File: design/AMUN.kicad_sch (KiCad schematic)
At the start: 18 parts, among them IC2 SHT40-AD1B-R2, IC3 SGP40-D-R4, J6 SFV12R-1STBE1HLF, Q2 SSM3K16FV,L3F, U1 12P_ZIF_Connector, U2 ER-TFT018-3

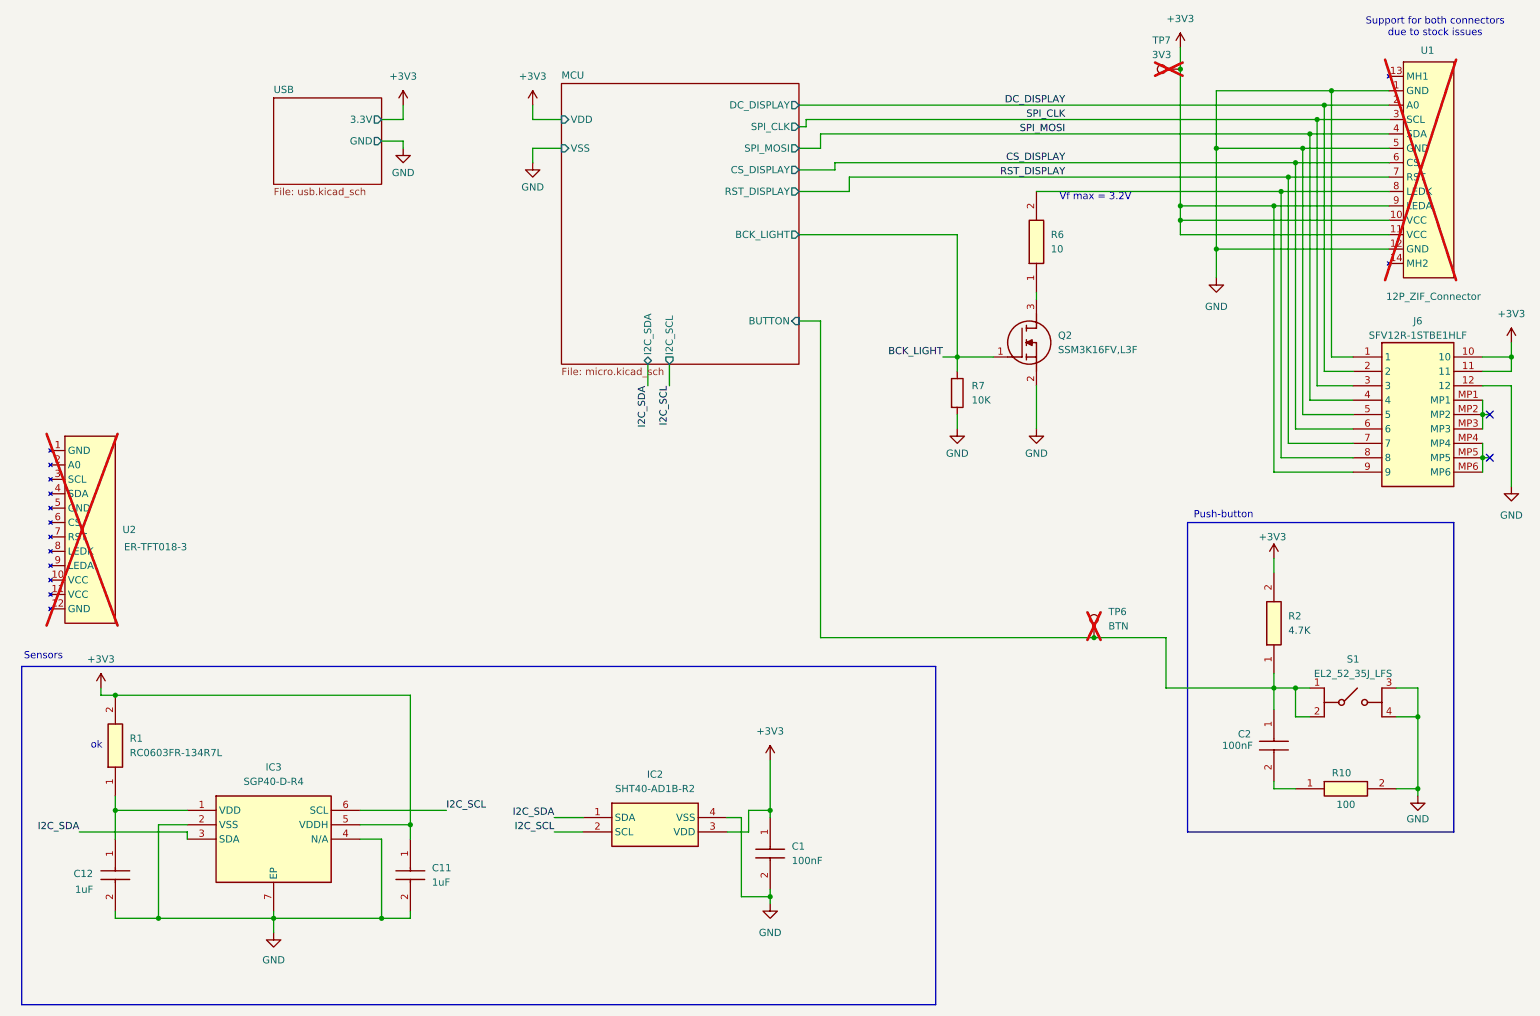
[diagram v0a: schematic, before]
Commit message: - Added display.kicad_sch; - Added mounting holes on schematic; - Removed TAG connect pads and used pin header; - Cut the PCB in order to make space for USB connector; - Changed mounting holes foorprint to non-plated ones; - Cut board near SHT4x sensor in order to reduce heat contribution from the rest of the board; - Re-routing; - Added revision number on silkscreen; - Shrunk components ID on silkscreen.
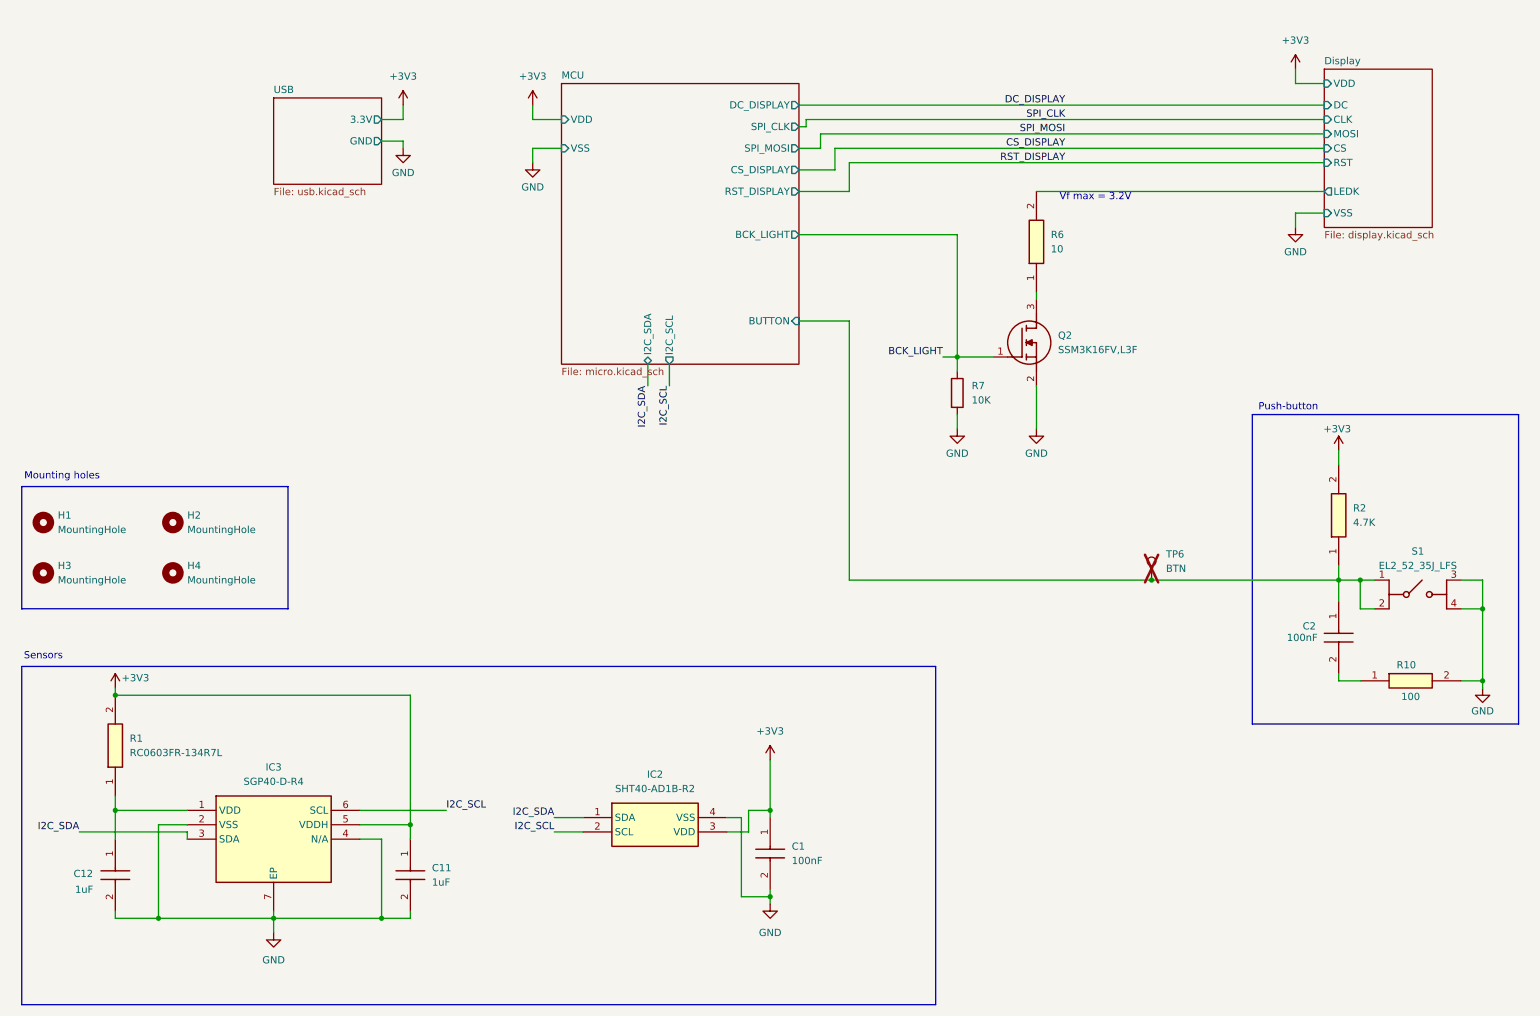
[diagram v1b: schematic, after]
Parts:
- removed J6: SFV12R-1STBE1HLF, amun_lib:SFV12R1STBE1HLF, symbol SFV12R-1STBE1HLF:SFV12R-1STBE1HLF
- removed TP7: 3V3, TestPoint:TestPoint_Pad_D1.0mm, symbol Connector:TestPoint
- removed U1: 12P_ZIF_Connector, amun_lib:ER-CON12HB-1, symbol amun_lib:12P_ZIF_Connector
- removed U2: ER-TFT018-3, amun_lib:ER-TFT018-3, symbol amun_lib:ER-TFT018-3
- added H1, H2, H3, H4: MountingHole, MountingHole:MountingHole_2.2mm_M2_DIN965, symbol Mechanical:MountingHole
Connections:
- net Display/LEDK: now reaches R6.2
- no-connect marks 2 -> 0
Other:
- added sheet Display (display.kicad_sch)
- note added: "Mounting holes"
- note removed: "Support for both connectors due to stock issues"
- note removed: "ok"
- moved on the sheet: C2, R10, R2, S1, TP6
